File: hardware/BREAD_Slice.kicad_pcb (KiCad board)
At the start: 2 copper layers, 72.6 x 100 mm, 16 parts, among them J1 Conn_01x10_Female, J2 I2C_01x04

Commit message: Initial commit
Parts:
- removed C3, C4: 22uF, Capacitor_SMD:C_1206_3216Metric
- removed HS1: Heatsink_Pad, SparkFun-Fuse:Thermal Pad
- removed L1: 4.7uH, Inductor_SMD:L_1210_3225Metric
- added D2: D, Diode_SMD:D_1206_3216Metric_Pad1.42x1.75mm_HandSolder, B.Cu at (162.0, 77.3)
- added D3: D, Diode_SMD:D_1206_3216Metric_Pad1.42x1.75mm_HandSolder, B.Cu at (161.8, 62.3)
- added D4: D, Diode_SMD:D_1206_3216Metric_Pad1.42x1.75mm_HandSolder, B.Cu at (162.2, 91.5)
- added D5: D_Zener, Diode_SMD:D_1206_3216Metric_Pad1.42x1.75mm_HandSolder, B.Cu at (160.2, 127.7)
- added D6: D_Zener, Diode_SMD:D_1206_3216Metric_Pad1.42x1.75mm_HandSolder, B.Cu at (160.2, 120.9)
- added D7: D_Zener, Diode_SMD:D_1206_3216Metric_Pad1.42x1.75mm_HandSolder, B.Cu at (160.2, 113.9)
- added D8: D_Zener, Diode_SMD:D_1206_3216Metric_Pad1.42x1.75mm_HandSolder, B.Cu at (160.2, 106.5)
- added J3: Screw_Terminal_01x03, TerminalBlock_TE-Connectivity:TerminalBlock_TE_282834-3_1x03_P2.54mm_Horizontal, F.Cu at (187.1, 89.5)
- added J4: Screw_Terminal_01x03, TerminalBlock_TE-Connectivity:TerminalBlock_TE_282834-3_1x03_P2.54mm_Horizontal, F.Cu at (187.1, 74.3)
- added J5: Screw_Terminal_01x03, TerminalBlock_TE-Connectivity:TerminalBlock_TE_282834-3_1x03_P2.54mm_Horizontal, F.Cu at (187.1, 103.2)
- added J6: Screw_Terminal_01x04, TerminalBlock_TE-Connectivity:TerminalBlock_TE_282834-4_1x04_P2.54mm_Horizontal, F.Cu at (187.5, 123.9)
- added K1: G5Q-1, Relay_THT:Relay_SPDT_Omron-G5Q-1, F.Cu at (159.2, 52.4)
- added K2: G5Q-1, Relay_THT:Relay_SPDT_Omron-G5Q-1, F.Cu at (159.2, 66.6)
- added K3: G5Q-1, Relay_THT:Relay_SPDT_Omron-G5Q-1, F.Cu at (159.2, 81.4)
- added K4: G5Q-1, Relay_THT:Relay_SPDT_Omron-G5Q-1, F.Cu at (159.2, 95.6)
- added R1: 1k, Resistor_SMD:R_1206_3216Metric_Pad1.30x1.75mm_HandSolder, B.Cu at (149.5, 45.1)
- added R2: 1k, Resistor_SMD:R_1206_3216Metric_Pad1.30x1.75mm_HandSolder, B.Cu at (149.8, 72.5)
- added R3: 1k, Resistor_SMD:R_1206_3216Metric_Pad1.30x1.75mm_HandSolder, B.Cu at (149.9, 58.5)
- added R4: 1k, Resistor_SMD:R_1206_3216Metric_Pad1.30x1.75mm_HandSolder, B.Cu at (149.7, 85.7)
- added RV1: 10k, Potentiometer_THT:Potentiometer_Bourns_3266W_Vertical, F.Cu at (175.4, 122.5)
- added RV2: 10k, Potentiometer_THT:Potentiometer_Bourns_3266W_Vertical, F.Cu at (166.2, 115.3)
- added RV3: 10k, Potentiometer_THT:Potentiometer_Bourns_3266W_Vertical, F.Cu at (175.1, 107.5)
- added RV4: 10k, Potentiometer_THT:Potentiometer_Bourns_3266W_Vertical, F.Cu at (166.5, 101.4)
- added U2: TCMT1100, Package_SO:SOP-4_4.4x2.6mm_P1.27mm, B.Cu at (149.8, 77.4)
- added U3: TCMT1100, Package_SO:SOP-4_4.4x2.6mm_P1.27mm, B.Cu at (149.9, 63.0)
- added U4: TCMT1100, Package_SO:SOP-4_4.4x2.6mm_P1.27mm, B.Cu at (149.8, 90.3)
- C1: value 22uF -> 10uF_t; footprint Capacitor_SMD:C_1206_3216Metric -> OCI_UPL_FOOTPRINTS:C_2312
- C2: value 100nF -> 10uF_t; footprint Capacitor_SMD:C_1206_3216Metric -> OCI_UPL_FOOTPRINTS:C_2312
- D1: value WS2812B_5050 -> D; footprint SparkFun-LED:WS2812-5050-4PIN -> Diode_SMD:D_1206_3216Metric_Pad1.42x1.75mm_HandSolder; moved to B.Cu
- H1, H4: footprint MountingHole:MountingHole_5mm -> MountingHole:MountingHole_3.2mm_M3_DIN965_Pad
- H2: renamed from H3; footprint MountingHole:MountingHole_5mm -> MountingHole:MountingHole_3.2mm_M3_DIN965_Pad
- H3: renamed from H2; footprint MountingHole:MountingHole_5mm -> MountingHole:MountingHole_3.2mm_M3_DIN965_Pad
- J2: value I2C_01x04 -> Screw_Terminal_01x03; footprint Connector_JST:JST_SH_SM04B-SRSS-TB_1x04-1MP_P1.00mm_Horizontal -> TerminalBlock_TE-Connectivity:TerminalBlock_TE_282834-3_1x03_P2.54mm_Horizontal; moved to F.Cu
- U1: value ~ -> TCMT1100; footprint Package_TO_SOT_SMD:TSOT-23-6 -> Package_SO:SOP-4_4.4x2.6mm_P1.27mm
- moved D1 88.0 mm to (162.2, 48.9), turned to -90 degrees
- moved J2 84.8 mm to (187.1, 60.0), turned to -90 degrees
- moved U1 76.2 mm to (149.7, 49.5)
- moved Logo1 75.1 mm to (166.6, 135.8), turned to 0 degrees
- moved C1 40.1 mm to (134.8, 79.9), turned to 90 degrees
- moved C2 31.5 mm to (154.6, 105.3), turned to 90 degrees
- moved A1 7.59 mm to (135.0, 100.0)
- moved J1 3.43 mm to (129.6, 78.8)
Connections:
- A1 pad 12: unconnected-(A1-D9-Pad12) -> /SW2
- A1 pad 13: unconnected-(A1-D10-Pad13) -> /SW3
- A1 pad 14: unconnected-(A1-D11-Pad14) -> /SW4
- A1 pad 19: unconnected-(A1-A0-Pad19) -> /A_IN1
- A1 pad 20: unconnected-(A1-A1-Pad20) -> /A_IN2
- A1 pad 21: unconnected-(A1-A2-Pad21) -> /A_IN3
- A1 pad 22: unconnected-(A1-A3-Pad22) -> /A_IN4
- A1 pad 30: unconnected-(A1-VIN-Pad30) -> +12V
- A1 pad 8: /LED -> unconnected-(A1-Pad8)
- A1 pad 9: unconnected-(A1-D6-Pad9) -> /SW1
- C1 pad 1: GND -> +12V
- C1 pad 2: +12V -> GND
- C2 pad 1: Net-(U1-SW) -> +5V
- C2 pad 2: Net-(U1-BST) -> GND
- D1 pad 2: unconnected-(D1-DOUT-Pad2) -> Net-(D1-Pad2)
- J2 pad 1: GND -> Net-(J2-Pad1)
- J2 pad 2: +5V -> Net-(J2-Pad2)
- J2 pad 3: /I2C_DAT -> Net-(J2-Pad3)
- U1 pad 1: +5V -> Net-(R1-Pad2)
- U1 pad 2: +12V -> GND
- U1 pad 3: +12V -> GND
- U1 pad 4: GND -> Net-(D1-Pad2)
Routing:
- net GND: track 19.6 -> 149.3 mm, vias 14 -> 3
- net /SW1: track 0.00 -> 83.7 mm
- net /SW2: track 0.00 -> 81.2 mm
- net /SW3: track 0.00 -> 68.5 mm
- net /SW4: track 0.00 -> 57.3 mm
- net /LED: track 51.5 -> 0.00 mm
- net +12V: track 46.8 -> 87.5 mm, vias 0 -> 2
- net /A_IN3: track 0.00 -> 32.6 mm
- net /I2C_CLK: track 78.5 -> 46.7 mm
- net /A_IN1: track 0.00 -> 31.7 mm
- net /I2C_DAT: track 76.6 -> 47.0 mm
- net /F_4: track 0.00 -> 28.1 mm
- net /A_IN4: track 0.00 -> 27.4 mm
- net Net-(J2-Pad3): track 0.00 -> 25.3 mm
- net Net-(J3-Pad3): track 0.00 -> 24.6 mm
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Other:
- board size 72.6 x 100 mm -> 70 x 100 mm
- board text added: "1"
- board text added: "2"
- board text added: "3"
- board text added: "4"
- board text added: "IN"
- board text added: "NC"
- board text added: "NO"
- board text added: "Relay 1"
- board text added: "Relay 2"
- board text added: "Relay 3"
- board text added: "Relay 4"
- board text added: "Relay Slice SLC_RLAY R0 2021"
- board text added: "Voltage IN"
- board text removed: "12V->5V Reg"
- board text removed: "5V I2C Connector"
- board text removed: "BREAD Slice Template SLC_TEMP <version> <year>"
- board text removed: "LED"

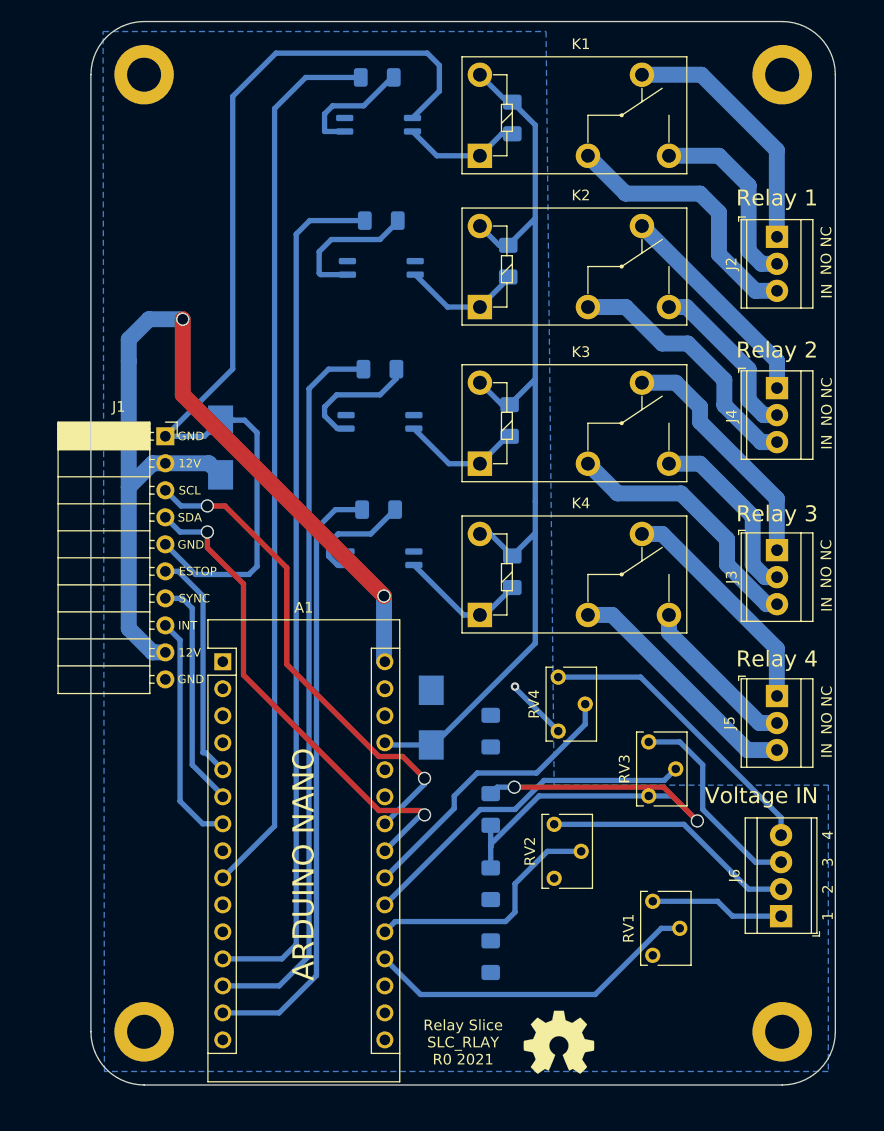
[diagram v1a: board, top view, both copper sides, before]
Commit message: added firmware and the updated PCB with new BREAD format
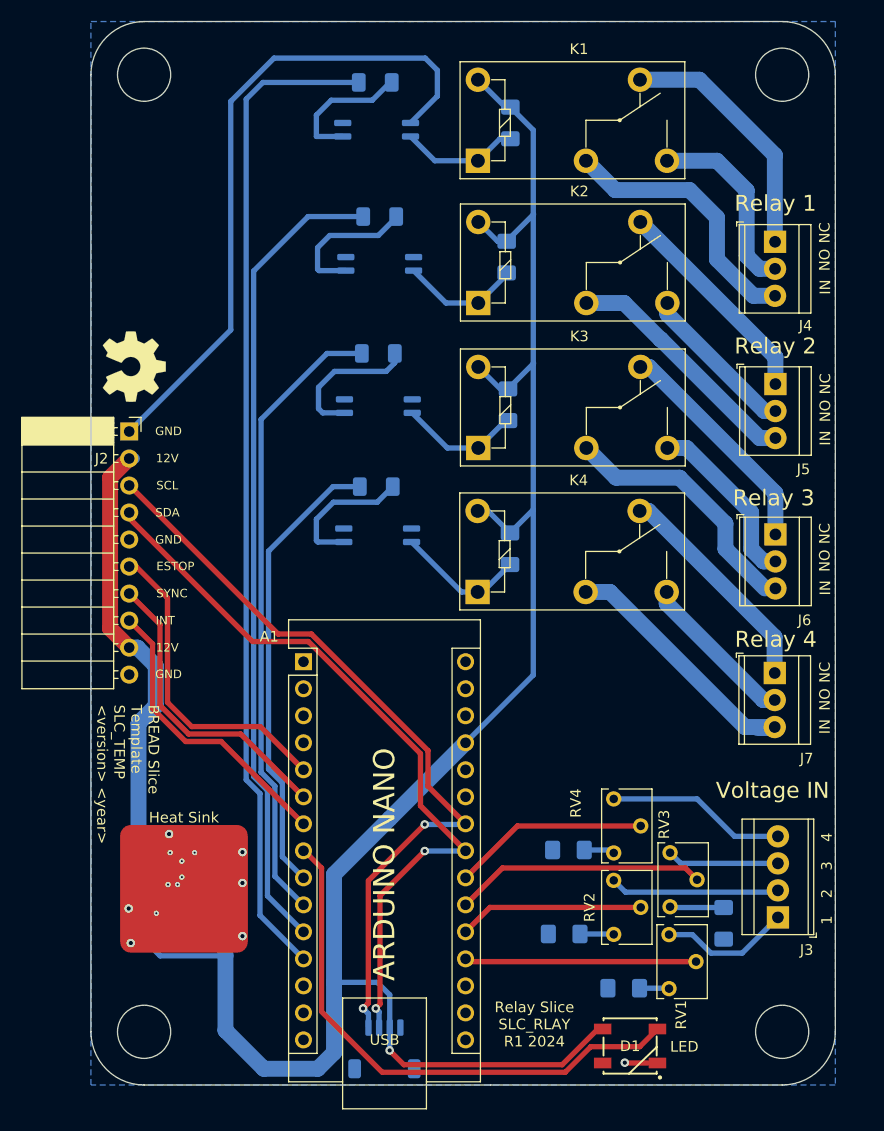
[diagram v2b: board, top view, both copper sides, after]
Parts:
- removed the J2 at (187.1, 60.0)
- added C3: 22uF, Capacitor_SMD:C_1206_3216Metric, B.Cu at (133.8, 119.5)
- added C4: 22uF, Capacitor_SMD:C_1206_3216Metric, B.Cu at (133.8, 116.5)
- added D9: D, Diode_SMD:D_1206_3216Metric_Pad1.42x1.75mm_HandSolder, B.Cu at (162.0, 89.4)
- added HS1: Heatsink_Pad, KML-Custom:Thermal Pad, F.Cu at (131.3, 121.4)
- added J1: I2C_01x04, Connector_JST:JST_SH_SM04B-SRSS-TB_1x04-1MP_P1.00mm_Horizontal, B.Cu at (150.2, 136.4)
- added J7: Screw_Terminal_01x03, TerminalBlock_TE-Connectivity:TerminalBlock_TE_282834-3_1x03_P2.54mm_Horizontal, F.Cu at (186.9, 101.1)
- added L1: 4.7uH, Inductor_SMD:L_1210_3225Metric, B.Cu at (133.8, 122.8)
- added U5: TCMT1100, Package_SO:SOP-4_4.4x2.6mm_P1.27mm, B.Cu at (149.6, 88.1)
- C1: value 10uF_t -> 22uF; footprint OCI_UPL_FOOTPRINTS:C_2312 -> Capacitor_SMD:C_1206_3216Metric
- C2: value 10uF_t -> 100nF; footprint OCI_UPL_FOOTPRINTS:C_2312 -> Capacitor_SMD:C_1206_3216Metric
- D1: value D -> WS2812B_5050; footprint Diode_SMD:D_1206_3216Metric_Pad1.42x1.75mm_HandSolder -> SparkFun-LED:WS2812-5050-4PIN; moved to F.Cu
- D2, D3, D4: value D -> D_Zener
- D6, D7, D8: value D_Zener -> D
- H1, H4: footprint MountingHole:MountingHole_3.2mm_M3_DIN965_Pad -> MountingHole:MountingHole_5mm
- H2: renamed from H3; footprint MountingHole:MountingHole_3.2mm_M3_DIN965_Pad -> MountingHole:MountingHole_5mm
- H3: renamed from H2; footprint MountingHole:MountingHole_3.2mm_M3_DIN965_Pad -> MountingHole:MountingHole_5mm
- J3: value Screw_Terminal_01x03 -> Screw_Terminal_01x04; footprint TerminalBlock_TE-Connectivity:TerminalBlock_TE_282834-3_1x03_P2.54mm_Horizontal -> TerminalBlock_TE-Connectivity:TerminalBlock_TE_282834-4_1x04_P2.54mm_Horizontal
- J6: value Screw_Terminal_01x04 -> Screw_Terminal_01x03; footprint TerminalBlock_TE-Connectivity:TerminalBlock_TE_282834-4_1x04_P2.54mm_Horizontal -> TerminalBlock_TE-Connectivity:TerminalBlock_TE_282834-3_1x03_P2.54mm_Horizontal
- U1: value TCMT1100 -> ~; footprint Package_SO:SOP-4_4.4x2.6mm_P1.27mm -> Package_TO_SOT_SMD:TSOT-23-6
- moved D1 88.0 mm to (173.3, 136.1), turned to 0 degrees
- moved U1 76.2 mm to (128.8, 122.8)
- moved Logo1 75.1 mm to (126.7, 72.2), turned to -90 degrees
- moved D6 71.6 mm to (162.0, 49.3)
- moved D3 63.5 mm to (167.1, 125.6), turned to 180 degrees
- moved D2 54.5 mm to (172.7, 130.7), turned to 180 degrees
- moved D7 52.0 mm to (161.7, 62.0)
- moved C1 40.1 mm to (128.6, 119.5), turned to 180 degrees
- moved D4 38.6 mm to (182.1, 124.6)
- moved J6 35.9 mm to (187.0, 88.0), turned to -90 degrees
- moved J3 34.5 mm to (187.2, 124.0), turned to 90 degrees
- moved C2 31.5 mm to (131.2, 126.3), turned to 180 degrees
- moved D8 30.7 mm to (161.8, 75.8)
- moved J5 29.3 mm to (187.0, 73.9)
- moved U2 27.5 mm to (149.5, 50.0)
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- renumbered J1 to J2
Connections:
- A1 pad 10: unconnected-(A1-Pad10) -> /SW3
- A1 pad 11: unconnected-(A1-Pad11) -> /SW2
- A1 pad 12: /SW2 -> /SW1
- A1 pad 13: /SW3 -> unconnected-(A1-D10-Pad13)
- A1 pad 14: /SW4 -> unconnected-(A1-D11-Pad14)
- A1 pad 30: +12V -> unconnected-(A1-VIN-Pad30)
- A1 pad 8: unconnected-(A1-Pad8) -> /LED
- A1 pad 9: /SW1 -> /SW4
- C1 pad 1: +12V -> GND
- C1 pad 2: GND -> +12V
- C2 pad 1: +5V -> Net-(U1-SW)
- C2 pad 2: GND -> Net-(U1-BST)
- D1 pad 2: Net-(D1-Pad2) -> unconnected-(D1-DOUT-Pad2)
- D2 pad 1: +5V -> GND
- D2 pad 2: Net-(D2-Pad2) -> GND
- D3 pad 1: +5V -> GND
- D3 pad 2: Net-(D3-Pad2) -> GND
- D4 pad 1: +5V -> GND
- D4 pad 2: Net-(D4-Pad2) -> GND
- D6 pad 1: GND -> +5V
- D6 pad 2: GND -> Net-(D6-A)
- D7 pad 1: GND -> +5V
- D7 pad 2: GND -> Net-(D7-A)
- D8 pad 1: GND -> +5V
- D8 pad 2: GND -> Net-(D8-A)
- J3 pad 1: Net-(J3-Pad1) -> /F_1
- J3 pad 2: Net-(J3-Pad2) -> /F_2
- J3 pad 3: Net-(J3-Pad3) -> /F_3
- J4 pad 1: Net-(J4-Pad1) -> /Relay1/NC
- J4 pad 2: Net-(J4-Pad2) -> /Relay1/NO
- J4 pad 3: Net-(J4-Pad3) -> /Relay1/IN
- J5 pad 1: Net-(J5-Pad1) -> /Relay2/NC
- J5 pad 2: Net-(J5-Pad2) -> /Relay2/NO
- J5 pad 3: Net-(J5-Pad3) -> /Relay2/IN
- J6 pad 1: /F_1 -> /Relay3/NC
- J6 pad 2: /F_2 -> /Relay3/NO
- J6 pad 3: /F_3 -> /Relay3/IN
- K1 pad 1: Net-(D1-Pad2) -> Net-(D6-A)
- K1 pad 2: Net-(J2-Pad3) -> /Relay1/IN
- K1 pad 3: Net-(J2-Pad2) -> /Relay1/NO
- K1 pad 4: Net-(J2-Pad1) -> /Relay1/NC
- K2 pad 1: Net-(D3-Pad2) -> Net-(D7-A)
- K2 pad 2: Net-(J4-Pad3) -> /Relay2/IN
- K2 pad 3: Net-(J4-Pad2) -> /Relay2/NO
- K2 pad 4: Net-(J4-Pad1) -> /Relay2/NC
- K3 pad 1: Net-(D2-Pad2) -> Net-(D8-A)
- K3 pad 2: Net-(J3-Pad3) -> /Relay3/IN
- K3 pad 3: Net-(J3-Pad2) -> /Relay3/NO
- K3 pad 4: Net-(J3-Pad1) -> /Relay3/NC
- K4 pad 1: Net-(D4-Pad2) -> Net-(D9-A)
- K4 pad 2: Net-(J5-Pad3) -> /Relay4/IN
- K4 pad 3: Net-(J5-Pad2) -> /Relay4/NO
- K4 pad 4: Net-(J5-Pad1) -> /Relay4/NC
- R2 pad 1: /SW3 -> /SW2
- R3 pad 1: /SW2 -> /SW3
- U1 pad 1: Net-(R1-Pad2) -> +5V
- U1 pad 2: GND -> +12V
- U1 pad 3: GND -> +12V
- U1 pad 4: Net-(D1-Pad2) -> GND
- U2 pad 1: Net-(R2-Pad2) -> Net-(R1-Pad2)
- U2 pad 4: Net-(D2-Pad2) -> Net-(D6-A)
- U3 pad 1: Net-(R3-Pad2) -> Net-(R2-Pad2)
- U3 pad 4: Net-(D3-Pad2) -> Net-(D7-A)
- U4 pad 1: Net-(R4-Pad2) -> Net-(R3-Pad2)
- U4 pad 4: Net-(D4-Pad2) -> Net-(D8-A)
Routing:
- net +5V: track 95.1 -> 196.6 mm, vias 0 -> 1
- net GND: track 149.3 -> 96.2 mm, vias 3 -> 14
- net /LED: track 0.00 -> 51.5 mm
- net +12V: track 87.5 -> 46.2 mm, vias 2 -> 0
- net /I2C_CLK: track 46.7 -> 72.3 mm
- net Net-(J2-Pad3): track 25.3 -> 0.00 mm
- net /Relay1/IN: track 0.00 -> 25.3 mm
- net /Relay4/IN: track 0.00 -> 24.7 mm
- net Net-(J3-Pad3): track 24.6 -> 0.00 mm
- net Net-(J4-Pad3): track 24.4 -> 0.00 mm
- net /Relay1/NC: track 0.00 -> 23.8 mm
- net Net-(J2-Pad1): track 23.8 -> 0.00 mm
- net /Relay3/IN: track 0.00 -> 23.7 mm
- net /I2C_DAT: track 47.0 -> 70.5 mm
- net /Relay2/IN: track 0.00 -> 23.0 mm
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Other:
- outline, holes or cut-outs redrawn
- board text added: "12V->5V Reg"
- board text added: "5V I2C Connector"
- board text added: "BREAD Slice Template SLC_TEMP <version> <year>"
- board text added: "LED"
- board text added: "Relay Slice SLC_RLAY R1 2024"
- board text removed: "Relay Slice SLC_RLAY R0 2021"

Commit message: changed terminals to meet those of the relays max output with margin
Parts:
- J3: footprint TerminalBlock_TE-Connectivity:TerminalBlock_TE_282834-4_1x04_P2.54mm_Horizontal -> TerminalBlock_Phoenix:TerminalBlock_Phoenix_MPT-0,5-4-2.54_1x04_P2.54mm_Horizontal
- J4, J5, J6, J7: footprint TerminalBlock_TE-Connectivity:TerminalBlock_TE_282834-3_1x03_P2.54mm_Horizontal -> TerminalBlock_Phoenix:TerminalBlock_Phoenix_MKDS-1,5-3-5.08_1x03_P5.08mm_Horizontal
- R1, R2, R3, R4: value 1k -> 180
- moved J4 6.81 mm to (186.8, 53.7)
- moved J5 3.68 mm to (186.8, 70.2)
- moved J3 3.20 mm to (188.1, 127.1)
- moved J7 2.54 mm to (186.8, 103.6)
- moved J6 1.24 mm to (186.8, 86.8)
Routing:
- net /Relay2/IN: track 23.0 -> 38.5 mm
- net /Relay1/NC: track 23.8 -> 16.9 mm
- net /Relay1/NO: track 18.0 -> 12.5 mm
- net /Relay4/NO: track 15.0 -> 19.4 mm
- net /Relay2/NC: track 20.5 -> 17.3 mm
- net /Relay4/IN: track 24.7 -> 27.6 mm
- net /Relay3/IN: track 23.7 -> 26.4 mm
- net /F_4: track 16.9 -> 19.1 mm
- net /F_3: track 10.6 -> 12.7 mm
- net /F_2: track 16.0 -> 18.0 mm
- net /Relay4/NC: track 21.0 -> 23.0 mm
- net /Relay3/NC: track 21.5 -> 19.7 mm
- net /Relay1/IN: track 25.3 -> 24.5 mm
- net /Relay3/NO: track 16.6 -> 17.2 mm

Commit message: JLCPCB order rev-A
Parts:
- added G***: LOGO, LOGO, F.Cu at (143.0, 63.1)
- moved D4 10.1 mm to (172.7, 128.2), turned to 0 degrees
- moved J7 1.71 mm to (185.8, 102.2)
- moved J6 1.35 mm to (185.8, 86.0)
- moved J5 1.19 mm to (185.7, 69.7)
- moved J4 1.11 mm to (185.7, 53.4)
- moved J3 0.30 mm to (187.8, 127.1)
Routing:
- net GND: track 96.2 -> 34.9 mm
- net /Relay2/IN: track 38.5 -> 22.2 mm
- net /Relay1/IN: track 24.5 -> 21.0 mm
- net /Relay3/NO: track 17.2 -> 14.8 mm
- net /Relay2/NO: track 14.6 -> 12.5 mm
- net /Relay1/NC: track 16.9 -> 14.9 mm
- net /Relay4/NO: track 19.4 -> 17.6 mm
- net /Relay4/NC: track 23.0 -> 21.2 mm
- net /Relay4/IN: track 27.6 -> 25.9 mm
- net /Relay3/IN: track 26.4 -> 25.1 mm
- net /Relay3/NC: track 19.7 -> 18.4 mm
- net /Relay2/NC: track 17.3 -> 16.0 mm
- net /Relay1/NO: track 12.5 -> 11.3 mm
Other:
- board text added: "BREAD Slice Relay I/O (SLC_RLAY) Cam K Brooks rev.A [09-2024]"
- board text removed: "BREAD Slice Template SLC_TEMP <version> <year>"
- board text removed: "Relay Slice SLC_RLAY R1 2024"
